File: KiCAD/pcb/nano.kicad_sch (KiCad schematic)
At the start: 24 parts, among them J1 Barrel_Jack_Switch, J2 Conn_01x02_Male, J3 Conn_01x02_Male, J4 Conn_01x04_Male, J5 Conn_01x03_Male, K1 SANYOU_SRD_Form_C, K2 SANYOU_SRD_Form_C, P1 Digital, P2 Analog, Q1 S8050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

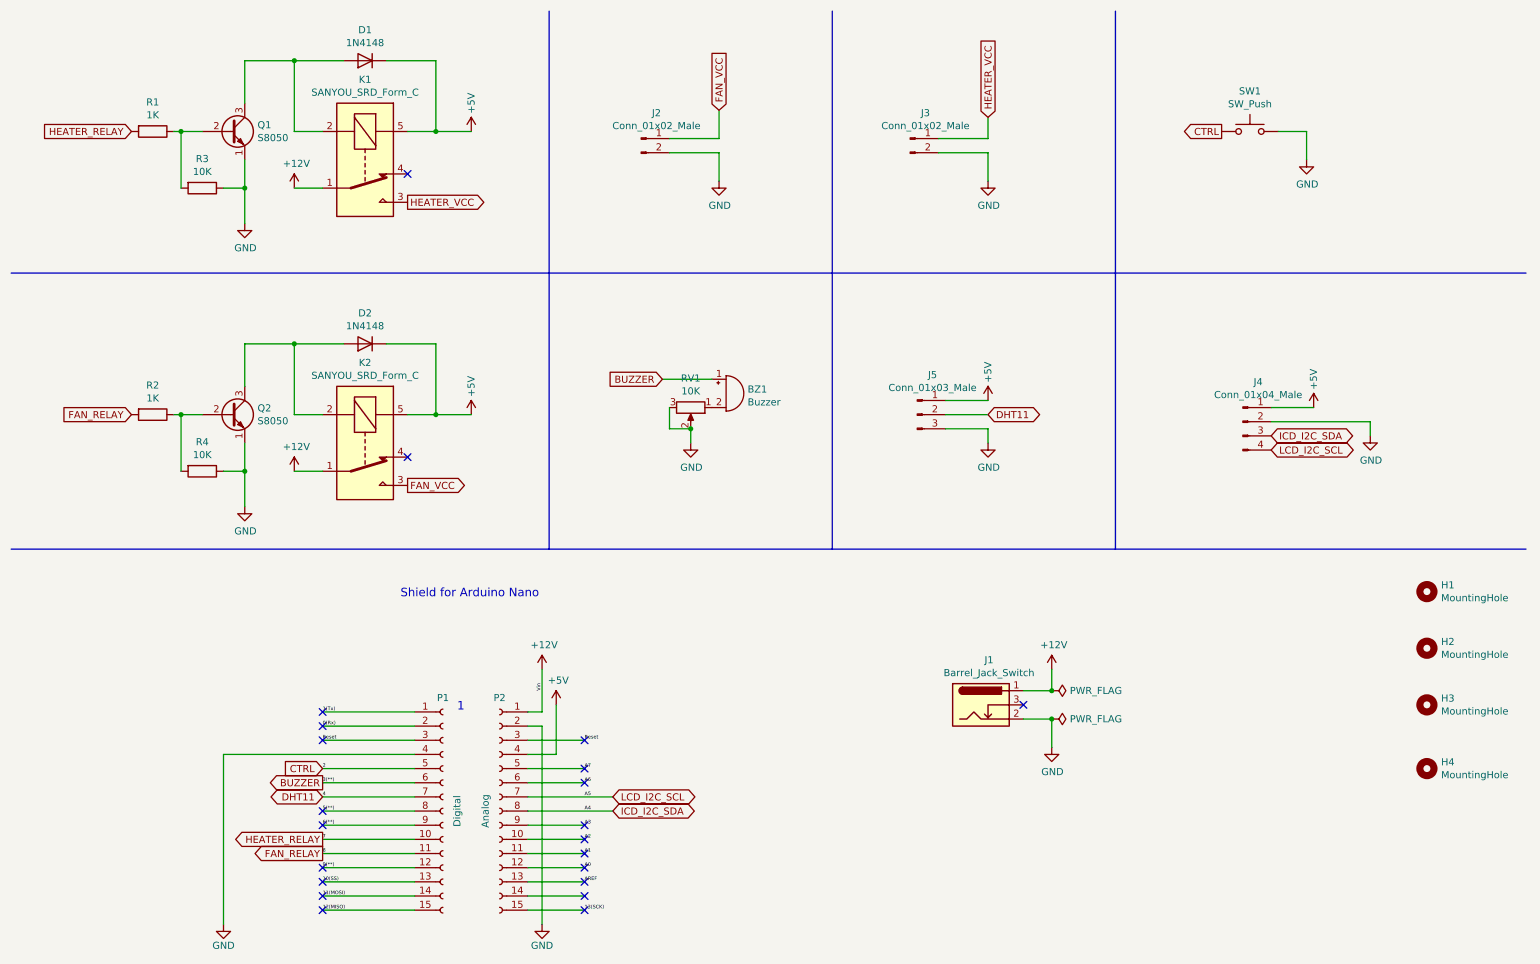
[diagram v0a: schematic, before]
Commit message: fixed LCD cable sequence
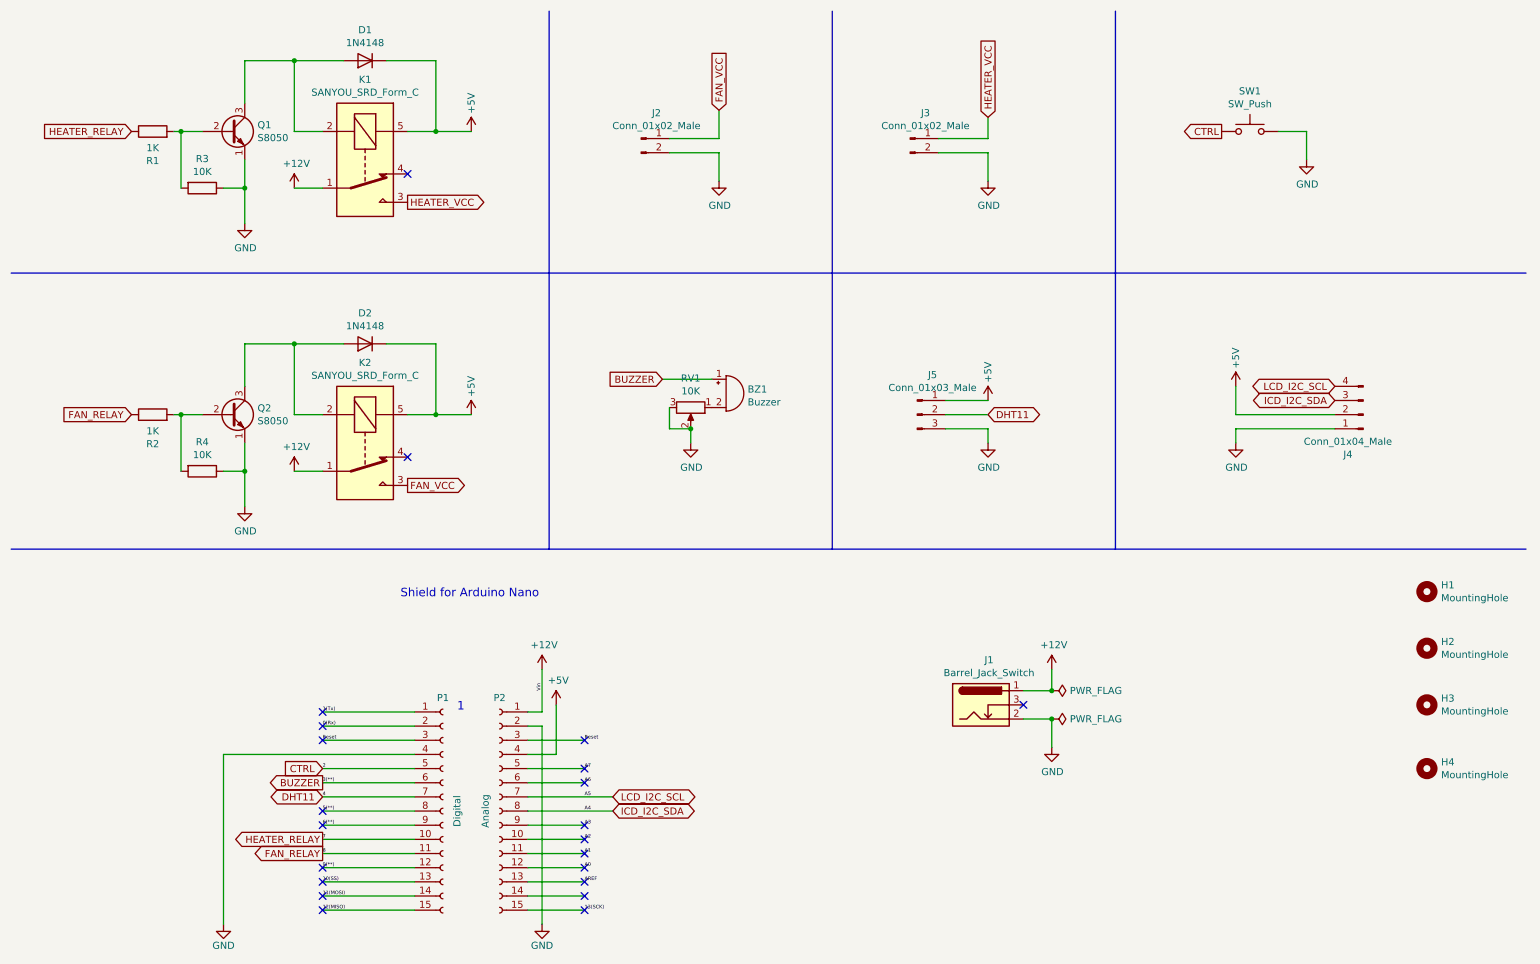
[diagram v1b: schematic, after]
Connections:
- net +5V: now also J4.2 (Pin_2); no longer J4.1 (Pin_1)
- net FAN_RELAY: now also R2.1; no longer R2.2
- net GND: now also J4.1 (Pin_1); no longer J4.2 (Pin_2)
- net HEATER_RELAY: now also R1.1; no longer R1.2
- net at Q2.2 (B), R4.2: now also R2.2; no longer R2.1
- net at Q1.2 (B), R3.2: now also R1.2; no longer R1.1
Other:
- moved on the sheet: J4, R1, R2
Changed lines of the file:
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@@
     (stroke (width 0) (type default) (color 0 0 0 0))
   )
-  (wire (pts (xy 238.76 83.82) (xy 246.38 83.82))
+  (wire (pts (xy 232.41 87.63) (xy 250.19 87.63))
+    (stroke (width 0) (type default) (color 0 0 0 0))
+  )
+  (wire (pts (xy 232.41 90.17) (xy 232.41 87.63))
     (stroke (width 0) (type default) (color 0 0 0 0))
   )
@@
     (stroke (width 0) (type default) (color 0 0 0 0))
   )
+  (wire (pts (xy 232.41 85.09) (xy 232.41 80.01))
+    (stroke (width 0) (type default) (color 0 0 0 0))
+  )
   (wire (pts (xy 85.09 156.21) (xy 68.58 156.21))
     (stroke (width 0) (type default) (color 0 0 0 0))
@@
     (stroke (width 0) (type default) (color 0 0 0 0))
   )
-  (wire (pts (xy 238.76 86.36) (xy 256.54 86.36))
-    (stroke (width 0) (type default) (color 0 0 0 0))
-  )
   (wire (pts (xy 240.03 34.29) (xy 245.11 34.29))
     (stroke (width 0) (type default) (color 0 0 0 0))
@@
     (stroke (width 0) (type default) (color 0 0 0 0))
   )
-  (wire (pts (xy 256.54 86.36) (xy 256.54 88.9))
-    (stroke (width 0) (type default) (color 0 0 0 0))
-  )
   (wire (pts (xy 105.41 173.99) (xy 115.57 173.99))
     (stroke (width 0) (type default) (color 0 0 0 0))
   )
   (wire (pts (xy 187.96 87.63) (xy 187.96 90.17))
+    (stroke (width 0) (type default) (color 0 0 0 0))
+  )
+  (wire (pts (xy 250.19 85.09) (xy 232.41 85.09))
     (stroke (width 0) (type default) (color 0 0 0 0))
   )
@@
     )
   )
-  (global_label "LCD_I2C_SCL" (shape bidirectional) (at 238.76 91.44 0) (fields_autoplaced)
-    (effects (font (size 1.27 1.27)) (justify left))
-    (property "Intersheet References" "${INTERSHEET_REFS}" (id 0) (at 0 0 0)
+  (global_label "LCD_I2C_SCL" (shape bidirectional) (at 250.19 80.01 180) (fields_autoplaced)
+    (effects (font (size 1.27 1.27)) (justify right))
+    (property "Intersheet References" "${INTERSHEET_REFS}" (id 0) (at 488.95 171.45 0)
       (effects (font (size 1.27 1.27)) hide)
     )
@@
     )
   )
-  (global_label "ICD_I2C_SDA" (shape bidirectional) (at 238.76 88.9 0) (fields_autoplaced)
-    (effects (font (size 1.27 1.27)) (justify left))
-    (property "Intersheet References" "${INTERSHEET_REFS}" (id 0) (at 0 0 0)
+  (global_label "ICD_I2C_SDA" (shape bidirectional) (at 250.19 82.55 180) (fields_autoplaced)
+    (effects (font (size 1.27 1.27)) (justify right))
+    (property "Intersheet References" "${INTERSHEET_REFS}" (id 0) (at 488.95 171.45 0)
       (effects (font (size 1.27 1.27)) hide)
     )
@@
     (pin "1")
   )
-  (symbol (lib_id "Device:R") (at 38.1 85.09 270) (unit 1)
-    (in_bom yes) (on_board yes)
-    (property "Reference" "R2" (id 0) (at 38.1 79.8322 90))
-    (property "Value" "1K" (id 1) (at 38.1 82.1436 90))
-    (property "Footprint" "Resistor_THT:R_Axial_DIN0204_L3.6mm_D1.6mm_P7.62mm_Horizontal" (id 2) (at 38.1 83.312 90)
+  (symbol (lib_id "Device:R") (at 38.1 85.09 90) (unit 1)
+    (in_bom yes) (on_board yes)
+    (property "Reference" "R2" (id 0) (at 38.1 90.3478 90))
+    (property "Value" "1K" (id 1) (at 38.1 88.0364 90))
+    (property "Footprint" "Resistor_THT:R_Axial_DIN0204_L3.6mm_D1.6mm_P7.62mm_Horizontal" (id 2) (at 38.1 86.868 90)
       (effects (font (size 1.27 1.27)) hide)
     )
@@
     (pin "1")
   )
-  (symbol (lib_id "Device:R") (at 38.1 34.29 270) (unit 1)
-    (in_bom yes) (on_board yes)
-    (property "Reference" "R1" (id 0) (at 38.1 29.0322 90))
-    (property "Value" "1K" (id 1) (at 38.1 31.3436 90))
-    (property "Footprint" "Resistor_THT:R_Axial_DIN0204_L3.6mm_D1.6mm_P7.62mm_Horizontal" (id 2) (at 38.1 32.512 90)
+  (symbol (lib_id "Device:R") (at 38.1 34.29 90) (unit 1)
+    (in_bom yes) (on_board yes)
+    (property "Reference" "R1" (id 0) (at 38.1 39.5478 90))
+    (property "Value" "1K" (id 1) (at 38.1 37.2364 90))
+    (property "Footprint" "Resistor_THT:R_Axial_DIN0204_L3.6mm_D1.6mm_P7.62mm_Horizontal" (id 2) (at 38.1 36.068 90)
       (effects (font (size 1.27 1.27)) hide)
     )
@@
     (pin "1")
   )
-  (symbol (lib_id "Connector:Conn_01x04_Male") (at 233.68 86.36 0) (unit 1)
-    (in_bom yes) (on_board yes)
-    (property "Reference" "J4" (id 0) (at 236.4232 79.2226 0))
-    (property "Value" "Conn_01x04_Male" (id 1) (at 236.4232 81.534 0))
-    (property "Footprint" "Connector_PinHeader_2.54mm:PinHeader_1x04_P2.54mm_Vertical" (id 2) (at 233.68 86.36 0)
-      (effects (font (size 1.27 1.27)) hide)
-    )
-    (property "Datasheet" "~" (id 3) (at 233.68 86.36 0)
+  (symbol (lib_id "Connector:Conn_01x04_Male") (at 255.27 85.09 180) (unit 1)
+    (in_bom yes) (on_board yes)
+    (property "Reference" "J4" (id 0) (at 252.5268 92.2274 0))
+    (property "Value" "Conn_01x04_Male" (id 1) (at 252.5268 89.916 0))
+    (property "Footprint" "Connector_PinHeader_2.54mm:PinHeader_1x04_P2.54mm_Vertical" (id 2) (at 255.27 85.09 0)
+      (effects (font (size 1.27 1.27)) hide)
+    )
+    (property "Datasheet" "~" (id 3) (at 255.27 85.09 0)
       (effects (font (size 1.27 1.27)) hide)
     )
@@
     (pin "4")
   )
-  (symbol (lib_id "power:GND") (at 256.54 88.9 0) (unit 1)
-    (in_bom yes) (on_board yes)
-    (property "Reference" "#PWR016" (id 0) (at 256.54 95.25 0)
-      (effects (font (size 1.27 1.27)) hide)
-    )
-    (property "Value" "GND" (id 1) (at 256.667 93.2942 0))
-    (property "Footprint" "" (id 2) (at 256.54 88.9 0)
-      (effects (font (size 1.27 1.27)) hide)
-    )
-    (property "Datasheet" "" (id 3) (at 256.54 88.9 0)
-      (effects (font (size 1.27 1.27)) hide)
-    )
-    (pin "1")
-  )
-  (symbol (lib_id "power:+5V") (at 246.38 83.82 0) (unit 1)
-    (in_bom yes) (on_board yes)
-    (property "Reference" "#PWR015" (id 0) (at 246.38 87.63 0)
-      (effects (font (size 1.27 1.27)) hide)
-    )
-    (property "Value" "+5V" (id 1) (at 246.38 78.74 90))
-    (property "Footprint" "" (id 2) (at 246.38 83.82 0)
-      (effects (font (size 1.27 1.27)) hide)
-    )
-    (property "Datasheet" "" (id 3) (at 246.38 83.82 0)
-      (effects (font (size 1.27 1.27)) hide)
-    )
+  (symbol (lib_id "power:GND") (at 232.41 90.17 0) (unit 1)
+    (in_bom yes) (on_board yes)
+    (property "Reference" "#PWR016" (id 0) (at 232.41 96.52 0)
+      (effects (font (size 1.27 1.27)) hide)
+    )
+    (property "Value" "GND" (id 1) (at 232.537 94.5642 0))
+    (property "Footprint" "" (id 2) (at 232.41 90.17 0)
+      (effects (font (size 1.27 1.27)) hide)
+    )
+    (property "Datasheet" "" (id 3) (at 232.41 90.17 0)
+      (effects (font (size 1.27 1.27)) hide)
+    )
+    (pin "1")
+  )
+  (symbol (lib_id "power:+5V") (at 232.41 80.01 0) (unit 1)
+    (in_bom yes) (on_board yes)
+    (property "Reference" "#PWR015" (id 0) (at 232.41 83.82 0)
+      (effects (font (size 1.27 1.27)) hide)
+    )
+    (property "Value" "+5V" (id 1) (at 232.41 74.93 90))
+    (property "Footprint" "" (id 2) (at 232.41 80.01 0)
+      (effects (font (size 1.27 1.27)) hide)
+    )
+    (property "Datasheet" "" (id 3) (at 232.41 80.01 0)
+      (effects (font (size 1.27 1.27)) hide)
+    )

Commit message: PCB rearranged
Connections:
- net Reset renamed Reset1
- net Reset1: no longer P2.3 (Pin_3)
- new net Reset2: P2.3 (Pin_3)
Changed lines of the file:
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@@
     (effects (font (size 0.635 0.635)) (justify left bottom))
   )
-  (label "Reset" (at 115.57 143.51 0)
+  (label "Reset2" (at 115.57 143.51 0)
     (effects (font (size 0.635 0.635)) (justify left bottom))
   )
@@
     (effects (font (size 0.635 0.635)) (justify left bottom))
   )
-  (label "Reset" (at 68.58 143.51 0)
+  (label "Reset1" (at 68.58 143.51 0)
     (effects (font (size 0.635 0.635)) (justify left bottom))
   )
